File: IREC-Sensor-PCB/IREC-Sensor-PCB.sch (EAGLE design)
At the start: 9 parts, among them J1 RASPBERRYPI-40-PIN-GPIO_PTH_N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, J2 BME280-I2C, J3 BME280-SPI, J4 MPU6050

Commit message: Updated Sensor PCB files
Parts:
- removed J7, J8: (no value), SparkFun-Connectors:CONN_04SCREW
- added D1: 200mA/100V/1V, SparkFun-DiscreteSemi:DIODE-1N4148
- added K1: RELAY-SPDT-JQX-15F, SparkFun-Electromechanical:RELAY-SPDT-JQX-15F
- J1: value RASPBERRYPI-40-PIN-GPIO_PTH_NO_SHROUD -> (none); device SparkFun-Connectors:RASPBERRYPI-40-PIN-GPIO_PTH_NO_SHROUD -> SparkFun-Connectors:CONN_07
- J2: value BME280-I2C -> (none); device SparkFun-Connectors:CONN_041X04_NO_SILK -> SparkFun-Connectors:CONN_06SILK_FEMALE_PTH
- J3: value BME280-SPI -> (none); device SparkFun-Connectors:CONN_06NO_SILK_NO_POP -> SparkFun-Connectors:CONN_04
- J4: value MPU6050 -> (none); device SparkFun-Connectors:CONN_10NO_SILK_PTH_FEMALE -> SparkFun-Connectors:CONN_04SCREW
- J5, J6: device SparkFun-Connectors:CONN_04SCREW -> SparkFun-Connectors:CONN_023.5MM
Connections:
- removed net VDD: J1.3.3V@1, J2.2, J4.1
- new net 3.3V: J1.2, J2.2
- new net 5V: J1.1, J2.1, J4.2
- new net AD_AGM: J3.4
- new net AD_HPT: J1.5
- new net CS_HPT: J1.7
- new net INT: J3.3
- new net N$1: D1.A, J5.2, K1.COIL2
- new net N$2: D1.C, J5.1, K1.COIL1
- new net N$3: J6.2, K1.NO
- new net N$4: J6.1, K1.MAIN
- new net PS0: J3.1
- new net PS1: J3.2
- new net RST: J2.6
- net GND: now also J1.3, J2.3, J4.1; no longer J1.GND@6, J2.1, J4.2
- net SCL: now also J1.4, J2.5, J4.4; no longer J1.SCL, J2.4, J4.5
- net SDA: now also J1.6, J2.4, J4.3; no longer J1.SDA, J2.3, J4.6
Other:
- note added: "BME280"
- note added: "BNO055"
- note added: "I2C_HDR"
- note added: "None Of Your Business Consulting"
- note added: "Relay"
- note removed: "!CS"
- note removed: "ASCL"
- note removed: "ASDA"
- note removed: "BME280 https://www.sparkfun.com/products/13676"
- note removed: "CLK"
- note removed: "GND"
- note removed: "I2C Headers"
- note removed: "INT"
- note removed: "MPU 6050 https://www.sparkfun.com/products/11028 Warning: Part is deprecated."
- note removed: "None Of Your Business consulting"
- note removed: "Raspberry Pi 4B If using I2C, try using only the first 6 pins!"
- note removed: "SCK"
- note removed: "SDI"
- note removed: "SDO"
- note removed: "SYNC"
- note removed: "VDD"
- note removed: "VIO"

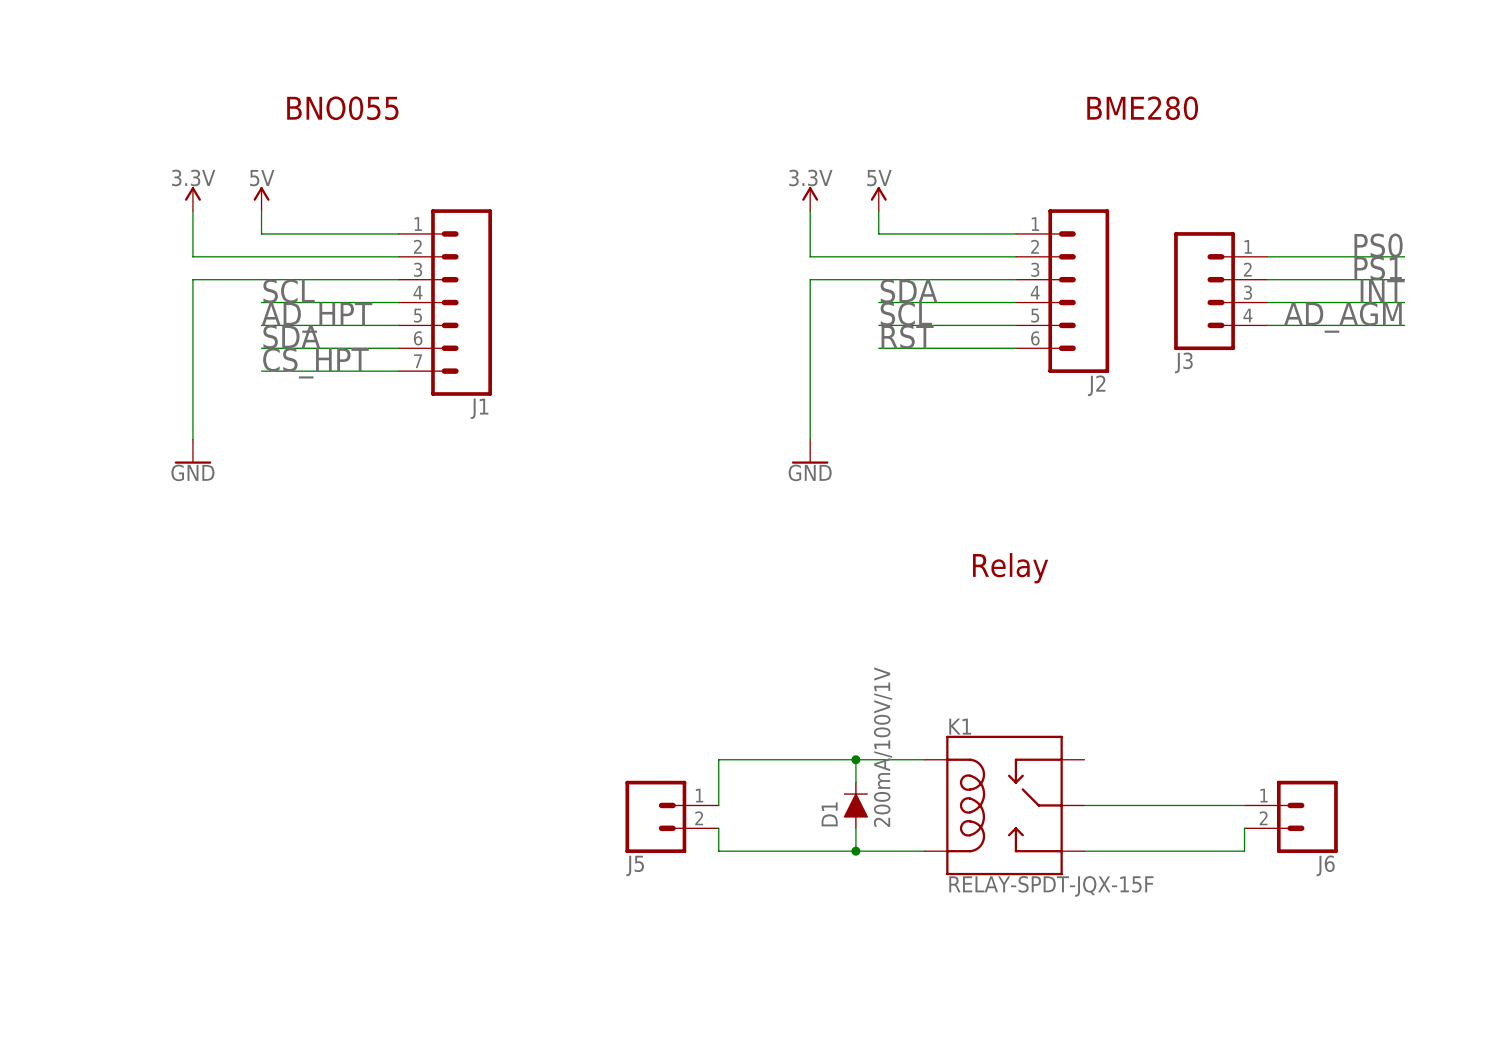
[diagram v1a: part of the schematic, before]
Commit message: Final 1.0.0 Board!
Board is complete!
- Adjusted board dimensions
- Added relay
- Added I2C address switches
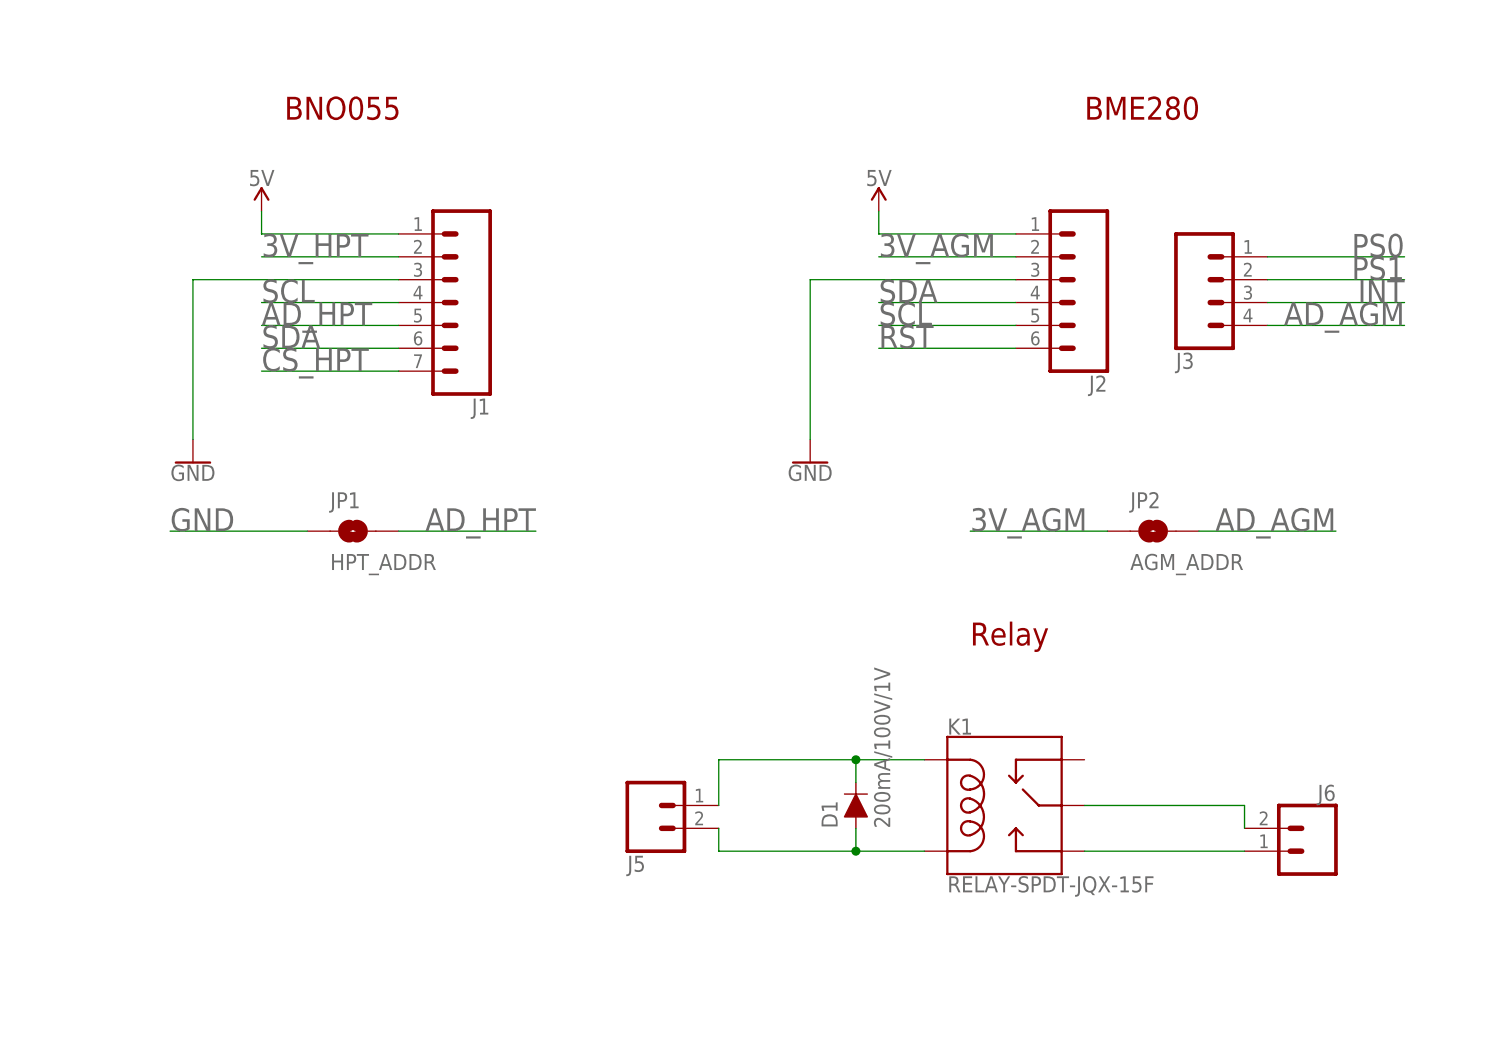
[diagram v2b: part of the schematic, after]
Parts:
- added JP1: HPT_ADDR, SparkFun-Jumpers:JUMPER-SMT_2_NO_SILK
- added JP2: AGM_ADDR, SparkFun-Jumpers:JUMPER-SMT_2_NO_SILK
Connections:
- removed net 3.3V: J1.2, J2.2
- new net 3V_AGM: J2.2, JP2.1
- new net 3V_HPT: J1.2
- net AD_AGM: now also JP2.2
- net AD_HPT: now also JP1.2
- net GND: now also JP1.1
- net N$3: now also K1.MAIN; no longer K1.NO
- net N$4: now also K1.NO; no longer K1.MAIN
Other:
- moved on the sheet: J6
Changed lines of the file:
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@@
 <part name="J3" library="SparkFun-Connectors" library_urn="urn:adsk.eagle:library:513" deviceset="CONN_04" device="" package3d_urn="urn:adsk.eagle:package:38085/1"/>
 <part name="SUPPLY1" library="SparkFun-PowerSymbols" library_urn="urn:adsk.eagle:library:530" deviceset="5V" device=""/>
-<part name="SUPPLY2" library="SparkFun-PowerSymbols" library_urn="urn:adsk.eagle:library:530" deviceset="3.3V" device=""/>
 <part name="GND1" library="SparkFun-PowerSymbols" library_urn="urn:adsk.eagle:library:530" deviceset="GND" device=""/>
 <part name="SUPPLY3" library="SparkFun-PowerSymbols" library_urn="urn:adsk.eagle:library:530" deviceset="5V" device=""/>
-<part name="SUPPLY4" library="SparkFun-PowerSymbols" library_urn="urn:adsk.eagle:library:530" deviceset="3.3V" device=""/>
 <part name="GND2" library="SparkFun-PowerSymbols" library_urn="urn:adsk.eagle:library:530" deviceset="GND" device=""/>
 <part name="J4" library="SparkFun-Connectors" library_urn="urn:adsk.eagle:library:513" deviceset="CONN_04" device="SCREW" package3d_urn="urn:adsk.eagle:package:38090/1"/>
@@
 <part name="J5" library="SparkFun-Connectors" library_urn="urn:adsk.eagle:library:513" deviceset="CONN_02" device="3.5MM" package3d_urn="urn:adsk.eagle:package:38050/1"/>
 <part name="J6" library="SparkFun-Connectors" library_urn="urn:adsk.eagle:library:513" deviceset="CONN_02" device="3.5MM" package3d_urn="urn:adsk.eagle:package:38050/1"/>
+<part name="JP1" library="SparkFun-Jumpers" library_urn="urn:adsk.eagle:library:528" deviceset="JUMPER-SMT_2_NO" device="_SILK" package3d_urn="urn:adsk.eagle:package:39279/1" value="HPT_ADDR"/>
+<part name="JP2" library="SparkFun-Jumpers" library_urn="urn:adsk.eagle:library:528" deviceset="JUMPER-SMT_2_NO" device="_SILK" package3d_urn="urn:adsk.eagle:package:39279/1" value="AGM_ADDR"/>
 </parts>
 <sheets>
@@
 <text x="129.54" y="149.86" size="2.54" layer="94">BME280</text>
 <text x="200.66" y="144.78" size="2.54" layer="94">I2C_HDR</text>
-<text x="116.84" y="99.06" size="2.54" layer="94">Relay</text>
+<text x="116.84" y="91.44" size="2.54" layer="94">Relay</text>
 </plain>
 <instances>
@@
 <attribute name="VALUE" x="38.1" y="142.494" size="1.778" layer="96" align="bottom-center"/>
 </instance>
-<instance part="SUPPLY2" gate="G$1" x="30.48" y="139.7" smashed="yes">
-<attribute name="VALUE" x="30.48" y="142.494" size="1.778" layer="96" align="bottom-center"/>
-</instance>
 <instance part="GND1" gate="1" x="30.48" y="111.76" smashed="yes">
 <attribute name="VALUE" x="30.48" y="111.506" size="1.778" layer="96" align="top-center"/>
@@
 <instance part="SUPPLY3" gate="G$1" x="106.68" y="139.7" smashed="yes">
 <attribute name="VALUE" x="106.68" y="142.494" size="1.778" layer="96" align="bottom-center"/>
-</instance>
-<instance part="SUPPLY4" gate="G$1" x="99.06" y="139.7" smashed="yes">
-<attribute name="VALUE" x="99.06" y="142.494" size="1.778" layer="96" align="bottom-center"/>
 </instance>
 <instance part="GND2" gate="1" x="99.06" y="111.76" smashed="yes">
@@
 <attribute name="NAME" x="78.74" y="68.072" size="1.778" layer="95" font="vector" rot="MR180"/>
 </instance>
-<instance part="J6" gate="G$1" x="154.94" y="73.66" smashed="yes" rot="R180">
-<attribute name="VALUE" x="157.48" y="78.486" size="1.778" layer="96" font="vector" rot="R180"/>
-<attribute name="NAME" x="157.48" y="68.072" size="1.778" layer="95" font="vector" rot="R180"/>
+<instance part="J6" gate="G$1" x="154.94" y="68.58" smashed="yes" rot="MR0">
+<attribute name="VALUE" x="157.48" y="63.754" size="1.778" layer="96" font="vector" rot="MR0"/>
+<attribute name="NAME" x="157.48" y="74.168" size="1.778" layer="95" font="vector" rot="MR0"/>
+</instance>
+<instance part="JP1" gate="G$1" x="48.26" y="104.14" smashed="yes">
+<attribute name="NAME" x="45.72" y="106.68" size="1.778" layer="95" font="vector"/>
+<attribute name="VALUE" x="45.72" y="101.6" size="1.778" layer="96" font="vector" align="top-left"/>
+</instance>
+<instance part="JP2" gate="G$1" x="137.16" y="104.14" smashed="yes">
+<attribute name="NAME" x="134.62" y="106.68" size="1.778" layer="95" font="vector"/>
+<attribute name="VALUE" x="134.62" y="101.6" size="1.778" layer="96" font="vector" align="top-left"/>
 </instance>
 </instances>
@@
 <label x="38.1" y="127" size="2.54" layer="95"/>
 </segment>
+<segment>
+<pinref part="JP1" gate="G$1" pin="2"/>
+<wire x1="53.34" y1="104.14" x2="68.58" y2="104.14" width="0.1524" layer="91"/>
+<label x="68.58" y="104.14" size="2.54" layer="95" rot="MR0"/>
+</segment>
 </net>
 <net name="SDA" class="0">
@@
 <label x="215.9" y="134.62" size="2.54" layer="95" rot="MR0"/>
 </segment>
-</net>
-<net name="3.3V" class="0">
-<segment>
-<pinref part="J1" gate="G$1" pin="2"/>
-<wire x1="53.34" y1="134.62" x2="30.48" y2="134.62" width="0.1524" layer="91"/>
-<pinref part="SUPPLY2" gate="G$1" pin="3.3V"/>
-<wire x1="30.48" y1="134.62" x2="30.48" y2="139.7" width="0.1524" layer="91"/>
-</segment>
-<segment>
-<wire x1="121.92" y1="134.62" x2="99.06" y2="134.62" width="0.1524" layer="91"/>
-<pinref part="SUPPLY4" gate="G$1" pin="3.3V"/>
-<wire x1="99.06" y1="134.62" x2="99.06" y2="139.7" width="0.1524" layer="91"/>
-<pinref part="J2" gate="G$1" pin="2"/>
+<segment>
+<pinref part="JP1" gate="G$1" pin="1"/>
+<wire x1="43.18" y1="104.14" x2="27.94" y2="104.14" width="0.1524" layer="91"/>
+<label x="27.94" y="104.14" size="2.54" layer="95"/>
 </segment>
 </net>
@@
 <wire x1="149.86" y1="127" x2="165.1" y2="127" width="0.1524" layer="91"/>
 <label x="165.1" y="127" size="2.54" layer="95" rot="MR0"/>
+</segment>
+<segment>
+<pinref part="JP2" gate="G$1" pin="2"/>
+<wire x1="142.24" y1="104.14" x2="157.48" y2="104.14" width="0.1524" layer="91"/>
+<label x="157.48" y="104.14" size="2.54" layer="95" rot="MR0"/>
 </segment>
 </net>
@@
 <net name="N$3" class="0">
 <segment>
+<pinref part="K1" gate="K$1" pin="MAIN"/>
+<pinref part="J6" gate="G$1" pin="2"/>
+<wire x1="129.54" y1="73.66" x2="147.32" y2="73.66" width="0.1524" layer="91"/>
+<wire x1="147.32" y1="73.66" x2="147.32" y2="71.12" width="0.1524" layer="91"/>
+</segment>
+</net>
+<net name="N$4" class="0">
+<segment>
 <pinref part="K1" gate="K$1" pin="NO"/>
-<pinref part="J6" gate="G$1" pin="2"/>
+<pinref part="J6" gate="G$1" pin="1"/>
 <wire x1="129.54" y1="68.58" x2="147.32" y2="68.58" width="0.1524" layer="91"/>
-<wire x1="147.32" y1="68.58" x2="147.32" y2="71.12" width="0.1524" layer="91"/>
-</segment>
-</net>
-<net name="N$4" class="0">
-<segment>
-<pinref part="K1" gate="K$1" pin="MAIN"/>
-<pinref part="J6" gate="G$1" pin="1"/>
-<wire x1="129.54" y1="73.66" x2="147.32" y2="73.66" width="0.1524" layer="91"/>
-</segment>
-</net>
+</segment>
+</net>
+<net name="3V_HPT" class="0">
+<segment>
+<pinref part="J1" gate="G$1" pin="2"/>
+<wire x1="53.34" y1="134.62" x2="38.1" y2="134.62" width="0.1524" layer="91"/>
+<label x="38.1" y="134.62" size="2.54" layer="95"/>
+</segment>
+</net>
+<net name="3V_AGM" class="0">
+<segment>
+<pinref part="J2" gate="G$1" pin="2"/>
+<wire x1="121.92" y1="134.62" x2="106.68" y2="134.62" width="0.1524" layer="91"/>
+<label x="106.68" y="134.62" size="2.54" layer="95"/>
+</segment>
+<segment>
+<pinref part="JP2" gate="G$1" pin="1"/>
+<wire x1="132.08" y1="104.14" x2="116.84" y2="104.14" width="0.1524" layer="91"/>
+<label x="116.84" y="104.14" size="2.54" layer="95"/>
+</segment>
+</net>
